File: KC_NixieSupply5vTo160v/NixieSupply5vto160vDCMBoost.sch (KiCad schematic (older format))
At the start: 45 parts, among them J1 Screw_Terminal_01x04, J2 CONN_01X01, J3 CONN_01X01, J4 CONN_01X01, J5 CONN_01X01, P1 USB_OTG, Q1 FDS2672CT, Q26 MMBT42, U1 UCC3803

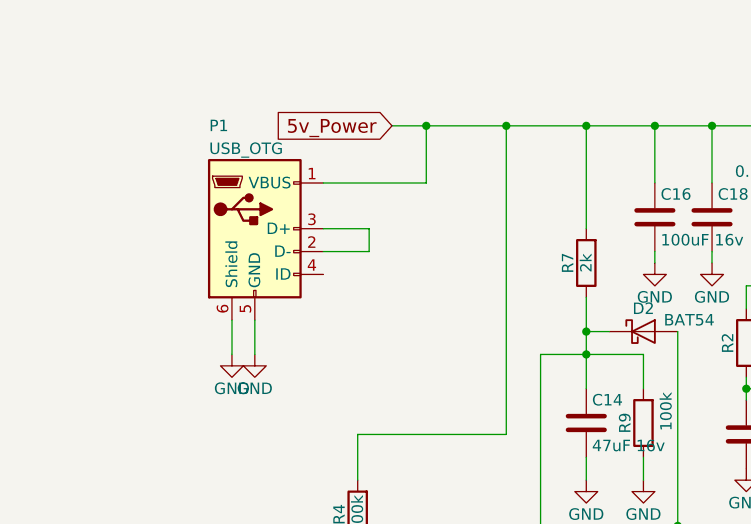
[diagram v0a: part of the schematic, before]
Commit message: New Rev 3 for the Original Nixie Power Supply 1. Corner Mounting Holes are now Solid.  Per the tip by comment reader 2. The original supply has a better ground connection for the USB input,     But the USB connector shield is still grounded. 2.5. The D+ and D- USB inputs are unshorted. 3. The revision was updated to Rev 3 for the Original Supply and Rev 2 for the Mini Supply 4. New Gerbers were created and zip files
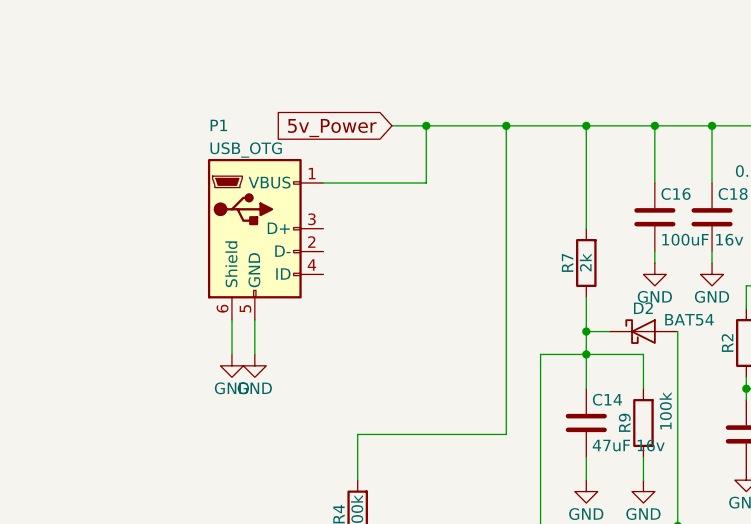
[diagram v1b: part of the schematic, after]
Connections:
- net at P1.2 (D-): no longer P1.3 (D+)
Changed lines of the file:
@@
-$EndComp
-$Comp
-L GND #PWR010
-U 1 1 5885B65A
-P 1500 3050
-F 0 "#PWR010" H 1500 2800 50  0001 C CNN
-F 1 "GND" H 1500 2900 50  0000 C CNN
-F 2 "" H 1500 3050 50  0000 C CNN
-F 3 "" H 1500 3050 50  0000 C CNN
-	1    1500 3050
-	1    0    0    -1
 $EndComp
 $Comp
@@
 $EndComp
 $Comp
-L GND #PWR011
+L GND #PWR010
 U 1 1 5960F6F8
 P 3350 2650
-F 0 "#PWR011" H 3350 2400 50  0001 C CNN
+F 0 "#PWR010" H 3350 2400 50  0001 C CNN
 F 1 "GND" H 3350 2500 50  0000 C CNN
 F 2 "" H 3350 2650 50  0000 C CNN
@@
 $EndComp
 $Comp
-L GND #PWR012
+L GND #PWR011
 U 1 1 59701877
 P 1600 3050
-F 0 "#PWR012" H 1600 2800 50  0001 C CNN
+F 0 "#PWR011" H 1600 2800 50  0001 C CNN
 F 1 "GND" H 1600 2900 50  0000 C CNN
 F 2 "" H 1600 3050 50  0000 C CNN
@@
 $EndComp
 $Comp
-L GND #PWR013
+L GND #PWR012
 U 1 1 597060B9
 P 7150 3100
-F 0 "#PWR013" H 7150 2850 50  0001 C CNN
+F 0 "#PWR012" H 7150 2850 50  0001 C CNN
 F 1 "GND" H 7150 2950 50  0000 C CNN
 F 2 "" H 7150 3100 50  0000 C CNN
@@
 $EndComp
 $Comp
-L GND #PWR014
+L GND #PWR013
 U 1 1 59706564
 P 7550 3100
-F 0 "#PWR014" H 7550 2850 50  0001 C CNN
+F 0 "#PWR013" H 7550 2850 50  0001 C CNN
 F 1 "GND" H 7550 2950 50  0000 C CNN
 F 2 "" H 7550 3100 50  0000 C CNN
@@
 $EndComp
 $Comp
-L GND #PWR015
+L GND #PWR014
 U 1 1 597066D0
 P 8150 3100
-F 0 "#PWR015" H 8150 2850 50  0001 C CNN
+F 0 "#PWR014" H 8150 2850 50  0001 C CNN
 F 1 "GND" H 8150 2950 50  0000 C CNN
 F 2 "" H 8150 3100 50  0000 C CNN
@@
 $EndComp
 $Comp
-L GND #PWR016
+L GND #PWR015
 U 1 1 597069A8
 P 8400 3100
-F 0 "#PWR016" H 8400 2850 50  0001 C CNN
+F 0 "#PWR015" H 8400 2850 50  0001 C CNN
 F 1 "GND" H 8400 2950 50  0000 C CNN
 F 2 "" H 8400 3100 50  0000 C CNN
@@
 $EndComp
 $Comp
-L GND #PWR017
+L GND #PWR016
 U 1 1 5A3FB941
 P 2350 4500
-F 0 "#PWR017" H 2350 4250 50  0001 C CNN
+F 0 "#PWR016" H 2350 4250 50  0001 C CNN
 F 1 "GND" H 2350 4350 50  0000 C CNN
 F 2 "" H 2350 4500 50  0000 C CNN
@@
 $EndComp
 $Comp
-L GND #PWR018
+L GND #PWR017
 U 1 1 5A408C45
 P 3050 3600
-F 0 "#PWR018" H 3050 3350 50  0001 C CNN
+F 0 "#PWR017" H 3050 3350 50  0001 C CNN
 F 1 "GND" H 3050 3450 50  0000 C CNN
 F 2 "" H 3050 3600 50  0000 C CNN
@@
 $EndComp
 $Comp
-L GND #PWR019
+L GND #PWR018
 U 1 1 5A409296
 P 3300 3600
-F 0 "#PWR019" H 3300 3350 50  0001 C CNN
+F 0 "#PWR018" H 3300 3350 50  0001 C CNN
 F 1 "GND" H 3300 3450 50  0000 C CNN
 F 2 "" H 3300 3600 50  0000 C CNN
@@
 $EndComp
 $Comp
-L GND #PWR020
+L GND #PWR019
 U 1 1 5A40B17A
 P 3600 2650
-F 0 "#PWR020" H 3600 2400 50  0001 C CNN
+F 0 "#PWR019" H 3600 2400 50  0001 C CNN
 F 1 "GND" H 3600 2500 50  0000 C CNN
 F 2 "" H 3600 2650 50  0000 C CNN
@@
 $EndComp
 $Comp
-L GND #PWR021
+L GND #PWR020
 U 1 1 5A460588
 P 9600 2900
-F 0 "#PWR021" H 9600 2650 50  0001 C CNN
+F 0 "#PWR020" H 9600 2650 50  0001 C CNN
 F 1 "GND" H 9600 2750 50  0000 C CNN
 F 2 "" H 9600 2900 50  0000 C CNN
@@
 	1600 3050 1600 2900
 Wire Wire Line
-	1500 2900 1500 3050
-Wire Wire Line
 	5200 3650 5200 4100
 Connection ~ 5200 4100
@@
 5v_Power
 $Comp
-L GND #PWR022
+L GND #PWR021
 U 1 1 5A46B11B
 P 5000 2700
-F 0 "#PWR022" H 5000 2450 50  0001 C CNN
+F 0 "#PWR021" H 5000 2450 50  0001 C CNN
 F 1 "GND" H 5000 2550 50  0000 C CNN
 F 2 "" H 5000 2700 50  0000 C CNN
@@
 	4600 5200 4600 5100
 $Comp
-L GND #PWR023
+L GND #PWR022
 U 1 1 5A47271C
 P 4600 5200
-F 0 "#PWR023" H 4600 4950 50  0001 C CNN
+F 0 "#PWR022" H 4600 4950 50  0001 C CNN
 F 1 "GND" H 4600 5050 50  0000 C CNN
 F 2 "" H 4600 5200 50  0000 C CNN
@@
 $EndComp
 $Comp
-L GND #PWR024
+L GND #PWR023
 U 1 1 5A4727AE
 P 4600 4700
-F 0 "#PWR024" H 4600 4450 50  0001 C CNN
+F 0 "#PWR023" H 4600 4450 50  0001 C CNN
 F 1 "GND" H 4600 4550 50  0000 C CNN
 F 2 "" H 4600 4700 50  0000 C CNN
@@
 $EndComp
 $Comp
-L GND #PWR025
+L GND #PWR024
 U 1 1 5A4786FA
 P 4300 2700
-F 0 "#PWR025" H 4300 2450 50  0001 C CNN
+F 0 "#PWR024" H 4300 2450 50  0001 C CNN
 F 1 "GND" H 4300 2550 50  0000 C CNN
 F 2 "" H 4300 2700 50  0000 C CNN
@@
 Wire Wire Line
 	4300 3050 4100 3050
-Wire Wire Line
-	1900 2500 2100 2500
-Wire Wire Line
-	2100 2500 2100 2600
-Wire Wire Line
-	2100 2600 1900 2600
 Text Notes 7300 1950 0    60   ~ 0
 OUTPUT SET to 167Volts
@@
 	1    0    0    -1
 $EndComp
+$Comp
+L GND #PWR025
+U 1 1 5885B65A
+P 1500 3050
+F 0 "#PWR025" H 1500 2800 50  0001 C CNN
+F 1 "GND" H 1500 2900 50  0000 C CNN
+F 2 "" H 1500 3050 50  0000 C CNN
+F 3 "" H 1500 3050 50  0000 C CNN
+	1    1500 3050
+	1    0    0    -1
+$EndComp
+Wire Wire Line
+	1500 2900 1500 3050
 $EndSCHEMATC

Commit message: The NewOrigin Zip file was used for the PCBWAY order This BOM was used for the PCBway order Updated the files to Rev 5 of Kicad
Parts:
- C1, C10, C11, C12, C13, C14, C15, C16, C18, C2, C3, C4, C5, C6, C7, C8: symbol C -> NixieSupply5vto160vDCMBoost-rescue:C
- D1: symbol D -> NixieSupply5vto160vDCMBoost-rescue:D
- D2: symbol D_Schottky -> NixieSupply5vto160vDCMBoost-rescue:D_Schottky
- J1: symbol Screw_Terminal_01x04 -> NixieSupply5vto160vDCMBoost-rescue:Screw_Terminal_01x04
- J2, J3, J4, J5: symbol Conn_01x01 -> NixieSupply5vto160vDCMBoost-rescue:Conn_01x01
- L2, L3, L5: symbol L -> NixieSupply5vto160vDCMBoost-rescue:L
- P1: symbol USB_OTG -> NixieSupply5vto160vDCMBoost-rescue:USB_OTG
- Q1: symbol FDMS86255ET150 -> NixieSupply5vto160vDCMBoost-rescue:FDMS86255ET150
- Q26: symbol MMBT3904 -> NixieSupply5vto160vDCMBoost-rescue:MMBT3904
- R1, R10, R12, R15, R16, R2, R3, R4, R5, R6, R7, R8, R9: symbol R -> NixieSupply5vto160vDCMBoost-rescue:R
- TP12, TP14: symbol TEST_1P -> NixieSupply5vto160vDCMBoost-rescue:TEST_1P
- U1: symbol AAC243 -> NixieSupply5vto160vDCMBoost-rescue:AAC243
